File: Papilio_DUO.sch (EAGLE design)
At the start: 121 parts, among them IC1 FT2232H, SW1 SWITCH-2CH-6P-3010010P1, SW2 EVQQ2, T100 MOSFET-NCHANNELSMD, U1 ARDUINO_MEGA_SHIELD, U100 PCA9306, U101 ATMEGA32U4-XUMU, U2 LTC3419EMS, U3 93C46B, X1 12MHz, Y1 16MHz KX-7

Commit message: Papilio DUO V1.0
Submitted for PCB
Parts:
- added C35, C36: .1uF, GadgetFactory:C0603
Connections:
- net 3V3: now also C35.1, C36.1
- net GND: now also C35.2, C36.2
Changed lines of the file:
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@@
 <part name="FRAME7" library="frames" deviceset="TABL_L" device=""/>
 <part name="5V0_PWR1" library="Bogdan_Commons" deviceset="5V0" device=""/>
+<part name="C35" library="GadgetFactory" deviceset="C" device="0603" value=".1uF"/>
+<part name="C36" library="GadgetFactory" deviceset="C" device="0603" value=".1uF"/>
 </parts>
 <sheets>
@@
 <text x="-101.6" y="-33.02" size="2.1844" layer="91">This work is licensed under the Creative Commons Attribution-ShareAlike License.</text>
 <text x="-101.6" y="-35.56" size="1.27" layer="91">To view a copy of this license, visit http://creativecommons.org/ ; or, (b) send a letter to Creative Commons, 171 2nd Street, Suite 300, San Francisco, California, 94105, USA.</text>
-<text x="218.44" y="-40.64" size="1.778" layer="91">See more details at www.GadgetFactory.net</text>
+<text x="220.98" y="-40.64" size="1.778" layer="91">See more details at www.GadgetFactory.net</text>
 <text x="-368.3" y="-58.42" size="1.016" layer="91">This work is licensed under the Creative Commons Attribution Share-Alike License.</text>
 <text x="-368.3" y="-60.96" size="1.016" layer="91">To view a copy of this license, visit http://creativecommons.org/ ; or, (b) send a letter to Creative Commons, 171 2nd Street, Suite 300, San Francisco, California, 94105, USA.</text>
@@
 <instance part="3V3_PWR18" gate="A" x="35.56" y="81.28" rot="R90"/>
 <instance part="5V0_PWR1" gate="A" x="-50.8" y="119.38"/>
+<instance part="C35" gate="A" x="-180.34" y="167.64" rot="R270"/>
+<instance part="C36" gate="A" x="-137.16" y="167.64" rot="R270"/>
 </instances>
 <busses>
@@
 <junction x="-319.8876" y="2.54"/>
 </segment>
+<segment>
+<pinref part="C35" gate="A" pin="2"/>
+<wire x1="-180.34" y1="165.1" x2="-180.34" y2="160.02" width="0.1524" layer="91"/>
+</segment>
+<segment>
+<pinref part="C36" gate="A" pin="2"/>
+<wire x1="-137.16" y1="165.1" x2="-137.16" y2="160.02" width="0.1524" layer="91"/>
+</segment>
 </net>
 <net name="AD0-JTAG_TCK" class="0">
@@
 <pinref part="3V3_PWR18" gate="A" pin="3V3"/>
 </segment>
+<segment>
+<pinref part="C35" gate="A" pin="1"/>
+<wire x1="-180.34" y1="170.18" x2="-180.34" y2="172.72" width="0.1524" layer="91"/>
+</segment>
+<segment>
+<pinref part="C36" gate="A" pin="1"/>
+<wire x1="-137.16" y1="170.18" x2="-137.16" y2="172.72" width="0.1524" layer="91"/>
+</segment>
 </net>

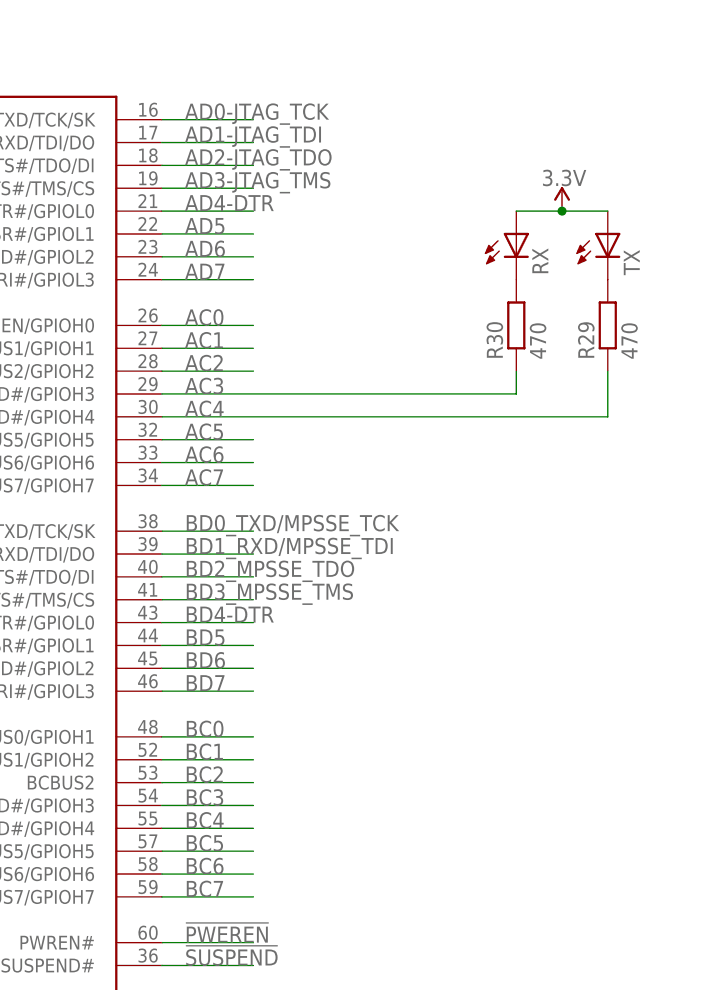
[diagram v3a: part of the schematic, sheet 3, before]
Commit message: Routing changes: VBUS connected, RX/TX LED's connected to port B instead of A.
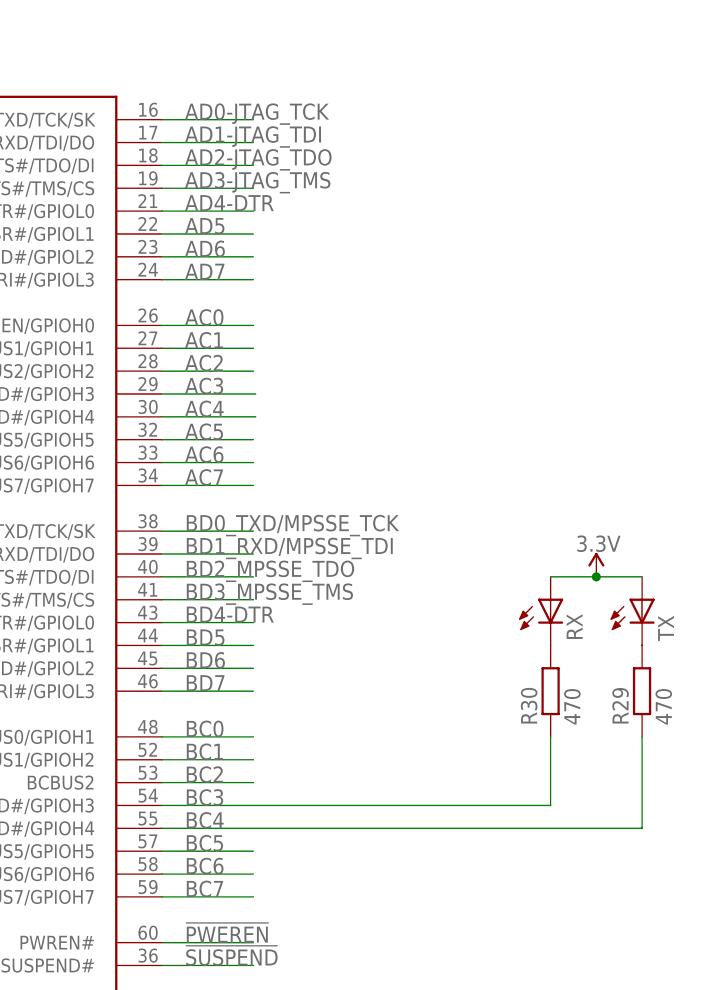
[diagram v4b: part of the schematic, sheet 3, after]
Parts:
- AVRUSB: PARTNO (none) -> 10118193-0001LF
- C1, C2: PARTNO (none) -> GRM21BR60J226ME39L
- C10, C101, C102, C105, C11, C12, C13, C15, C16, C17, C18, C20, C21, C22, C23, C24, C25, C26, C27, C29, C30, C31, C32, C33, C34, C35, C36, C4, C5, C6, C7: PARTNO (none) -> GRM188F51E104ZA01D
- C100: PARTNO (none) -> JMK105BJ105KV-F
- C103, C104: PARTNO (none) -> C1608X5R1A105K080AC
- C106, C107: PARTNO (none) -> C1608C0G1H220J080AA
- C14, C28: PARTNO (none) -> T491A475M010AT
- C19: PARTNO (none) -> T491A335K016AT7280
- C3: PARTNO (none) -> C0805C106K9PACTU
- C8, C9: PARTNO (none) -> CL10C270JB8NNNC
- FLASH: PARTNO (none) -> MX25L6445EM2I-10G
- FPGAUSB: PARTNO (none) -> USB-M26FTR
- HDMI: PARTNO (none) -> 10029449-001RLF
- IC1: PARTNO (none) -> FT2232HL-REEL
- L1, L2: PARTNO (none) -> VLS3015T-3R3M1R2
- L100: PARTNO (none) -> MH2029-300YCT-ND
- L3, L4: PARTNO (none) -> MMZ1608R600A
- LED, RX, TX: PARTNO (none) -> LTST-C170KGKT
- OSC: PARTNO (none) -> ASV-32.000MHZ-E-T
- PWR: PARTNO (none) -> LTST-C171EKT
- PWRIN: PARTNO (none) -> 68000-102HLF
- PWRSEL: PARTNO (none) -> 68000-103HLF
- R1, R22: PARTNO (none) -> RMCF0805JT22R0
- R10, R11, R12, R13, R14, R15, R16, R17, R18, R19, R20, R21, R8, R9: PARTNO (none) -> RMCF0603JT390R
- R100, R101: PARTNO (none) -> RMCF0402JT10K0
- R102: PARTNO (none) -> RMCF0402ZT0R00
- R103, R104, R106, R107: PARTNO (none) -> RMCF0402JT1K00
- R105: PARTNO (none) -> RMCF0402JT100K
- R108: PARTNO (none) -> RMCF0402JT2K20
- R109: PARTNO (none) -> RMCF0603JT1M00
- R110, R23, R24, R26, R28: PARTNO (none) -> RMCF0603JT10K0
- R2: PARTNO (none) -> CRCW06036K80FKEA
- R25: PARTNO (none) -> RMCF0603JT2K20
- R27: PARTNO (none) -> RMCF0603FT12K0
- R29, R30: PARTNO (none) -> RMCF0603JT470R
- R3, R4, R5: PARTNO (none) -> CRCW06031K50FKEA
- R31: PARTNO (none) -> RMCF0805JT47K0
- R32: PARTNO (none) -> RMCF0603JT4K70
- R6: PARTNO (none) -> RMCF0603JT1K80
- R7: PARTNO (none) -> RMCF0603JT1K00
- S1: PARTNO (none) -> XC6SLX9-2TQG144C
- SRAM: PARTNO (none) -> IS61WV20488BLL-10TLI
- SW1: PARTNO (none) -> EG1271
- SW2: PARTNO (none) -> PTS525SM10SMTR LFS
- T100: PARTNO (none) -> AD1584BRTZ-REEL7
- U$1, U$2, U$3, U$4, U$5, U$6, U$8, U1: BOM (none) -> EXCLUDE
- U100: PARTNO (none) -> PCA9306USG
- U101: PARTNO (none) -> ATMEGA32U4RC-MUR
- U2: PARTNO (none) -> LTC3419EMS#PBF
- U3: PARTNO (none) -> 93C46BT-I/OT
- X1: PARTNO (none) -> ABM7-12.000MHZ-D2Y-T
- Y1: PARTNO (none) -> ABM8G-16.000MHZ-B4Y-T
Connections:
- net 5V_ARDUINO: now also U101.VBUS
- net AC3: no longer R30.1
- net AC4: no longer R29.1
- net BC3: now also R30.1
- net BC4: now also R29.1
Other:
- moved on the sheet: R29, R30, RX, TX

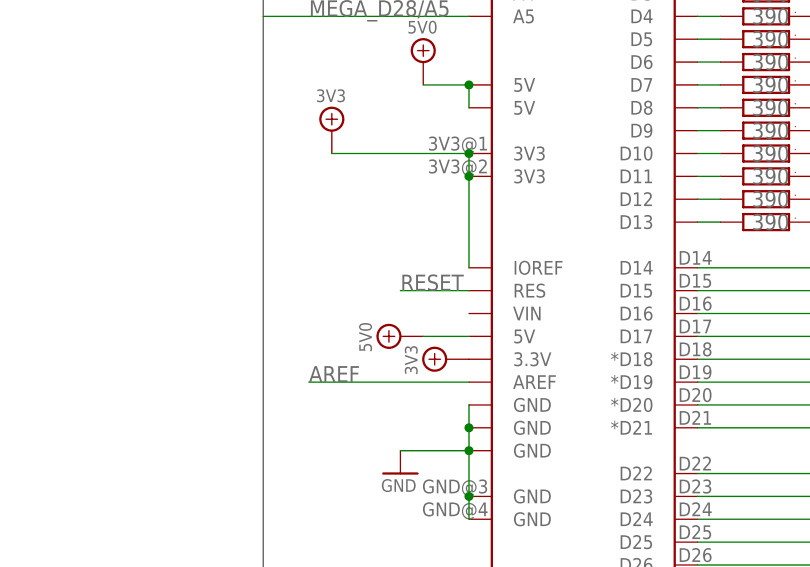
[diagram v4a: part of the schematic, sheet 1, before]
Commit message: Silkscreen fixes, Reset re-worked so RST pin resets atmega32u4 instead of FPGA.
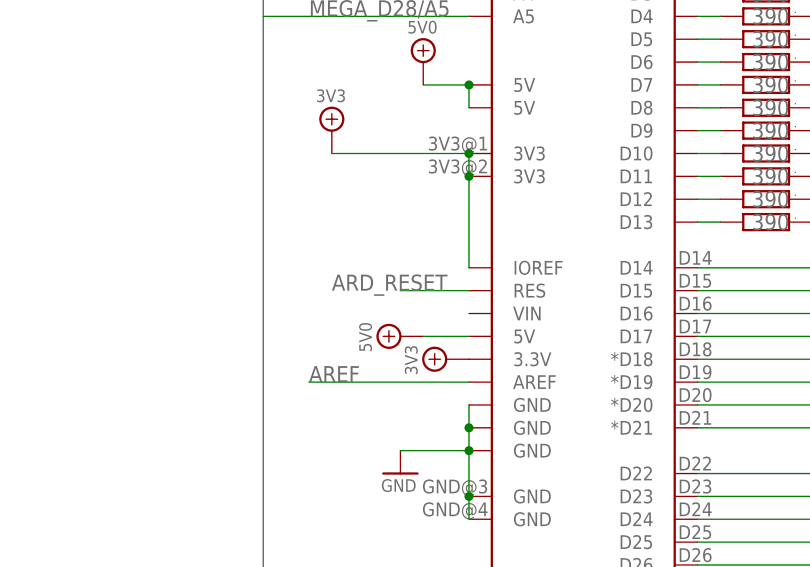
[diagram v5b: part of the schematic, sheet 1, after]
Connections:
- net ARD_RESET: now also U1.RES
- net RESET: no longer U1.RES
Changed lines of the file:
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@@
 <pinref part="R31" gate="A" pin="1"/>
-</segment>
-<segment>
-<wire x1="-45.72" y1="93.98" x2="-53.34" y2="93.98" width="0.2032" layer="91"/>
-<label x="-53.34" y="93.98" size="1.778" layer="95"/>
-<pinref part="U1" gate="ARDUINO_MEGA" pin="RES"/>
 </segment>
 </net>
@@
 <pinref part="S1" gate="B0" pin="IO_L3N_0"/>
 </segment>
-</net>
+<segment>
+<pinref part="U1" gate="ARDUINO_MEGA" pin="RES"/>
+<wire x1="-45.72" y1="93.98" x2="-53.34" y2="93.98" width="0.1524" layer="91"/>
+<label x="-60.96" y="93.98" size="1.778" layer="95"/>
+</segment>
+</net>

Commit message: Remove HDMI
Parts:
- removed C100: 1uF, saanlima:C0402
- removed HDMI: HDMI-TYPE-A-RECEPTICALFCI10029449, saanlima:HDMI-TYPE-A-RECEPTICALFCI10029449
- removed R100, R101: 10K, saanlima:R0402
- removed R102: 0, saanlima:R0402
- removed R103, R104, R106, R107: 1K, saanlima:R0402
- removed R105: 100K, saanlima:R0402
- removed R108: 2.2K, saanlima:R0402
- removed T100: MOSFET-NCHANNELSMD, saanlima:MOSFET-NCHANNELSMD
- removed U100: PCA9306, saanlima:PCA9306
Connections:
- removed net DDC_SCL: HDMI.SCL, R104.2, U100.SCL2
- removed net DDC_SDA: HDMI.SDA, R103.2, U100.SDA2
- removed net DETECT: HDMI.DETECT, R100.2, R101.1
- removed net HDMI_DET#: R108.2, T100.D
- removed net N$17: R101.2, T100.G
- removed net N$6: C100.1, R105.1, U100.EN, U100.VREF2
- removed net TX_HDMI_5V: HDMI.+5V, R102.1, R103.1, R104.1, R105.2
- net 3V3: no longer R106.1, R107.1, R108.1, U100.VREF1
- net 5V0: no longer R102.2
- net GND: no longer C100.2, HDMI.CLOCKSHIELD, HDMI.DATA0SHIELD, HDMI.DATA1SHIELD, HDMI.DATA2SHIELD, HDMI.DDC/CEC-GRND, HDMI.RES, R100.1, T100.S, U100.GND
- net MEGA_D43: no longer R106.2, U100.SDA1
- net MEGA_D44: no longer R107.2, U100.SCL1
- net MEGA_D45: no longer HDMI.DATA2+
- net MEGA_D46: no longer HDMI.DATA2-
- net MEGA_D47: no longer HDMI.DATA1+
- net MEGA_D48: no longer HDMI.DATA1-
- net MEGA_D49: no longer HDMI.DATA0+
- net MEGA_D50: no longer HDMI.DATA0-
- net MEGA_D51: no longer HDMI.CLOCK+
- net MEGA_D52: no longer HDMI.CLOCK-
- net MEGA_D53: no longer HDMI.CEC
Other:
- note removed: "Copyright Saanlima Electronics 2012"
- note removed: "Saanlima Electronics"
- note removed: "This section is from the Pipistrello design with permission from Magnus."

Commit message: Added Headers to the BOM
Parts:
- WING_POWER1, WING_POWER2, WING_POWER3, WING_POWER4, WING_POWER5, WING_POWER6: value POWER_ONLYNOTEXT -> HEADER_FEMALE_4; BOM EXCLUDE -> (none); PARTNO (none) -> PPTC041LFBN-RC
- renumbered U$2 to WING_POWER1, U$3 to WING_POWER4, U$4 to WING_POWER5, U$5 to WING_POWER3, U$6 to WING_POWER6, U$8 to WING_POWER2
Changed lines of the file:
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@@
 <setting verticaltext="up"/>
 </settings>
-<grid distance="0.1" unitdist="inch" unit="inch" style="lines" multiple="1" display="yes" altdistance="0.01" altunitdist="inch" altunit="inch"/>
+<grid distance="0.1" unitdist="inch" unit="inch" style="lines" multiple="1" display="no" altdistance="0.01" altunitdist="inch" altunit="inch"/>
 <layers>
 <layer number="1" name="Top" color="4" fill="1" visible="no" active="no"/>
@@
 <attribute name="PARTNO" value="PTS525SM10SMTR LFS"/>
 </part>
-<part name="U$2" library="Papilio" deviceset="POWER_ONLY" device="NOTEXT">
-<attribute name="BOM" value="EXCLUDE"/>
-</part>
-<part name="U$8" library="Papilio" deviceset="POWER_ONLY" device="NOTEXT">
-<attribute name="BOM" value="EXCLUDE"/>
-</part>
-<part name="U$5" library="Papilio" deviceset="POWER_ONLY" device="NOTEXT">
-<attribute name="BOM" value="EXCLUDE"/>
-</part>
-<part name="U$3" library="Papilio" deviceset="POWER_ONLY" device="NOTEXT">
-<attribute name="BOM" value="EXCLUDE"/>
-</part>
-<part name="U$4" library="Papilio" deviceset="POWER_ONLY" device="NOTEXT">
-<attribute name="BOM" value="EXCLUDE"/>
-</part>
-<part name="U$6" library="Papilio" deviceset="POWER_ONLY" device="NOTEXT">
-<attribute name="BOM" value="EXCLUDE"/>
+<part name="WING_POWER1" library="Papilio" deviceset="POWER_ONLY" device="NOTEXT" value="HEADER_FEMALE_4">
+<attribute name="PARTNO" value="PPTC041LFBN-RC"/>
+</part>
+<part name="WING_POWER2" library="Papilio" deviceset="POWER_ONLY" device="NOTEXT" value="HEADER_FEMALE_4">
+<attribute name="PARTNO" value="PPTC041LFBN-RC"/>
+</part>
+<part name="WING_POWER3" library="Papilio" deviceset="POWER_ONLY" device="NOTEXT" value="HEADER_FEMALE_4">
+<attribute name="PARTNO" value="PPTC041LFBN-RC"/>
+</part>
+<part name="WING_POWER4" library="Papilio" deviceset="POWER_ONLY" device="NOTEXT" value="HEADER_FEMALE_4">
+<attribute name="PARTNO" value="PPTC041LFBN-RC"/>
+</part>
+<part name="WING_POWER5" library="Papilio" deviceset="POWER_ONLY" device="NOTEXT" value="HEADER_FEMALE_4">
+<attribute name="PARTNO" value="PPTC041LFBN-RC"/>
+</part>
+<part name="WING_POWER6" library="Papilio" deviceset="POWER_ONLY" device="NOTEXT" value="HEADER_FEMALE_4">
+<attribute name="PARTNO" value="PPTC041LFBN-RC"/>
 </part>
 <part name="GND_PWR7" library="Bogdan_Commons" deviceset="GND" device=""/>
@@
 <part name="C36" library="GadgetFactory" deviceset="C" device="0603" value=".1uF">
 <attribute name="PARTNO" value="GRM188F51E104ZA01D"/>
+</part>
+<part name="HEADER_0-7" library="bom" deviceset="BOM-PART" device="" value="HEADER_FEMALE_8">
+<attribute name="PARTNO" value="PPTC081LFBN-RC"/>
+</part>
+<part name="HEADER_8-AREF" library="bom" deviceset="BOM-PART" device="" value="HEADER_FEMALE_8">
+<attribute name="PARTNO" value="PPTC081LFBN-RC"/>
+</part>
+<part name="HEADER_14-21" library="bom" deviceset="BOM-PART" device="" value="HEADER_FEMALE_8">
+<attribute name="PARTNO" value="PPTC081LFBN-RC"/>
+</part>
+<part name="HEADER_C" library="bom" deviceset="BOM-PART" device="" value="HEADER_FEMALE_19">
+<attribute name="PARTNO" value="PPTC191LFBN-RC"/>
+</part>
+<part name="HEADER_NC-IOREF" library="bom" deviceset="BOM-PART" device="" value="HEADER_FEMALE_7">
+<attribute name="PARTNO" value="PPTC071LFBN-RC"/>
+</part>
+<part name="HEADER_ANALOG" library="bom" deviceset="BOM-PART" device="" value="HEADER_FEMALE_6">
+<attribute name="PARTNO" value="PPTC061LFBN-RC"/>
+</part>
+<part name="HEADER_D" library="bom" deviceset="BOM-PART" device="" value="HEADER_FEMALE_19">
+<attribute name="PARTNO" value="PPTC191LFBN-RC"/>
 </part>
 </parts>
@@
 <attribute name="PARTNO" x="241.3" y="66.04" size="1.778" layer="96" display="off"/>
 </instance>
-<instance part="U$2" gate="G$1" x="-355.6" y="254">
-<attribute name="BOM" x="-355.6" y="254" size="1.778" layer="96" display="off"/>
-</instance>
-<instance part="U$8" gate="G$1" x="-337.82" y="254">
-<attribute name="BOM" x="-337.82" y="254" size="1.778" layer="96" display="off"/>
-</instance>
-<instance part="U$5" gate="G$1" x="-320.04" y="254">
-<attribute name="BOM" x="-320.04" y="254" size="1.778" layer="96" display="off"/>
-</instance>
-<instance part="U$3" gate="G$1" x="-302.26" y="254">
-<attribute name="BOM" x="-302.26" y="254" size="1.778" layer="96" display="off"/>
-</instance>
-<instance part="U$4" gate="G$1" x="-284.48" y="254">
-<attribute name="BOM" x="-284.48" y="254" size="1.778" layer="96" display="off"/>
-</instance>
-<instance part="U$6" gate="G$1" x="-266.7" y="254">
-<attribute name="BOM" x="-266.7" y="254" size="1.778" layer="96" display="off"/>
+<instance part="WING_POWER1" gate="G$1" x="-355.6" y="254">
+<attribute name="PARTNO" x="-355.6" y="254" size="1.778" layer="96" display="off"/>
+</instance>
+<instance part="WING_POWER2" gate="G$1" x="-337.82" y="254">
+<attribute name="PARTNO" x="-337.82" y="254" size="1.778" layer="96" display="off"/>
+</instance>
+<instance part="WING_POWER3" gate="G$1" x="-320.04" y="254">
+<attribute name="PARTNO" x="-320.04" y="254" size="1.778" layer="96" display="off"/>
+</instance>
+<instance part="WING_POWER4" gate="G$1" x="-302.26" y="254">
+<attribute name="PARTNO" x="-302.26" y="254" size="1.778" layer="96" display="off"/>
+</instance>
+<instance part="WING_POWER5" gate="G$1" x="-284.48" y="254">
+<attribute name="PARTNO" x="-284.48" y="254" size="1.778" layer="96" display="off"/>
+</instance>
+<instance part="WING_POWER6" gate="G$1" x="-266.7" y="254">
+<attribute name="PARTNO" x="-266.7" y="254" size="1.778" layer="96" display="off"/>
 </instance>
 <instance part="GND_PWR7" gate="A" x="-368.3" y="271.78"/>
@@
 <attribute name="PARTNO" x="-137.16" y="167.64" size="1.778" layer="96" display="off"/>
 </instance>
+<instance part="HEADER_0-7" gate="G$1" x="-96.52" y="-17.78"/>
+<instance part="HEADER_8-AREF" gate="G$1" x="-68.58" y="-17.78"/>
+<instance part="HEADER_14-21" gate="G$1" x="-40.64" y="-17.78"/>
+<instance part="HEADER_C" gate="G$1" x="-12.7" y="-17.78"/>
+<instance part="HEADER_NC-IOREF" gate="G$1" x="43.18" y="-17.78"/>
+<instance part="HEADER_ANALOG" gate="G$1" x="71.12" y="-17.78"/>
+<instance part="HEADER_D" gate="G$1" x="15.24" y="-17.78"/>
 </instances>
 <busses>
@@
 <wire x1="-287.02" y1="274.32" x2="-269.24" y2="274.32" width="0.2032" layer="91"/>
 <wire x1="-358.14" y1="274.32" x2="-368.3" y2="274.32" width="0.2032" layer="91"/>
-<pinref part="U$2" gate="G$1" pin="GND@P1"/>
-<pinref part="U$8" gate="G$1" pin="GND@P1"/>
-<pinref part="U$5" gate="G$1" pin="GND@P1"/>
-<pinref part="U$3" gate="G$1" pin="GND@P1"/>
-<pinref part="U$4" gate="G$1" pin="GND@P1"/>
-<pinref part="U$6" gate="G$1" pin="GND@P1"/>
+<pinref part="WING_POWER1" gate="G$1" pin="GND@P1"/>
+<pinref part="WING_POWER2" gate="G$1" pin="GND@P1"/>
+<pinref part="WING_POWER3" gate="G$1" pin="GND@P1"/>
+<pinref part="WING_POWER4" gate="G$1" pin="GND@P1"/>
+<pinref part="WING_POWER5" gate="G$1" pin="GND@P1"/>
+<pinref part="WING_POWER6" gate="G$1" pin="GND@P1"/>
 <pinref part="GND_PWR7" gate="A" pin="GND"/>
 </segment>
@@
 <wire x1="-287.02" y1="269.24" x2="-269.24" y2="269.24" width="0.2032" layer="91"/>
 <junction x="-358.14" y="269.24"/>
-<pinref part="U$2" gate="G$1" pin="3V3@P3"/>
-<pinref part="U$8" gate="G$1" pin="3V3@P3"/>
-<pinref part="U$5" gate="G$1" pin="3V3@P3"/>
-<pinref part="U$3" gate="G$1" pin="3V3@P3"/>
-<pinref part="U$4" gate="G$1" pin="3V3@P3"/>
-<pinref part="U$6" gate="G$1" pin="3V3@P3"/>
+<pinref part="WING_POWER1" gate="G$1" pin="3V3@P3"/>
+<pinref part="WING_POWER2" gate="G$1" pin="3V3@P3"/>
+<pinref part="WING_POWER3" gate="G$1" pin="3V3@P3"/>
+<pinref part="WING_POWER4" gate="G$1" pin="3V3@P3"/>
+<pinref part="WING_POWER5" gate="G$1" pin="3V3@P3"/>
+<pinref part="WING_POWER6" gate="G$1" pin="3V3@P3"/>
 <pinref part="3V3_PWR9" gate="A" pin="3V3"/>
 </segment>
@@
 <wire x1="-287.02" y1="266.7" x2="-269.24" y2="266.7" width="0.2032" layer="91"/>
 <junction x="-358.14" y="266.7"/>
-<pinref part="U$2" gate="G$1" pin="5V0@P4"/>
-<pinref part="U$8" gate="G$1" pin="5V0@P4"/>
-<pinref part="U$5" gate="G$1" pin="5V0@P4"/>
-<pinref part="U$3" gate="G$1" pin="5V0@P4"/>
-<pinref part="U$4" gate="G$1" pin="5V0@P4"/>
-<pinref part="U$6" gate="G$1" pin="5V0@P4"/>
+<pinref part="WING_POWER1" gate="G$1" pin="5V0@P4"/>
+<pinref part="WING_POWER2" gate="G$1" pin="5V0@P4"/>
+<pinref part="WING_POWER3" gate="G$1" pin="5V0@P4"/>
+<pinref part="WING_POWER4" gate="G$1" pin="5V0@P4"/>
+<pinref part="WING_POWER5" gate="G$1" pin="5V0@P4"/>
+<pinref part="WING_POWER6" gate="G$1" pin="5V0@P4"/>
 <pinref part="5V0_PWR4" gate="A" pin="5V0"/>
 </segment>
